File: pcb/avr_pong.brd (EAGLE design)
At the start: 61.3 x 58.4 mm, 20 parts, among them IC1 7805TV, J1 DCJ0202, U1 ATMEGA328P_PDIP, Y1 16 MHz

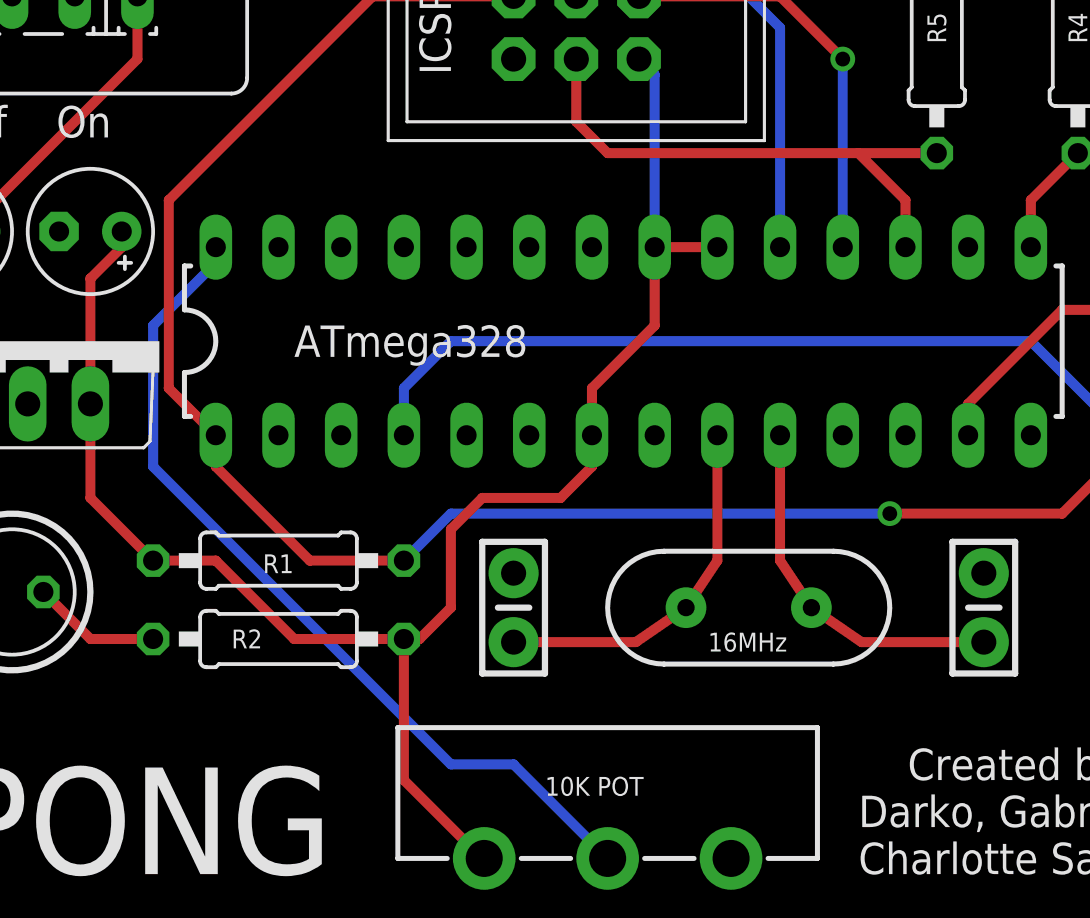
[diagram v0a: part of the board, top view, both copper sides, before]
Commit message: Updated board layout.
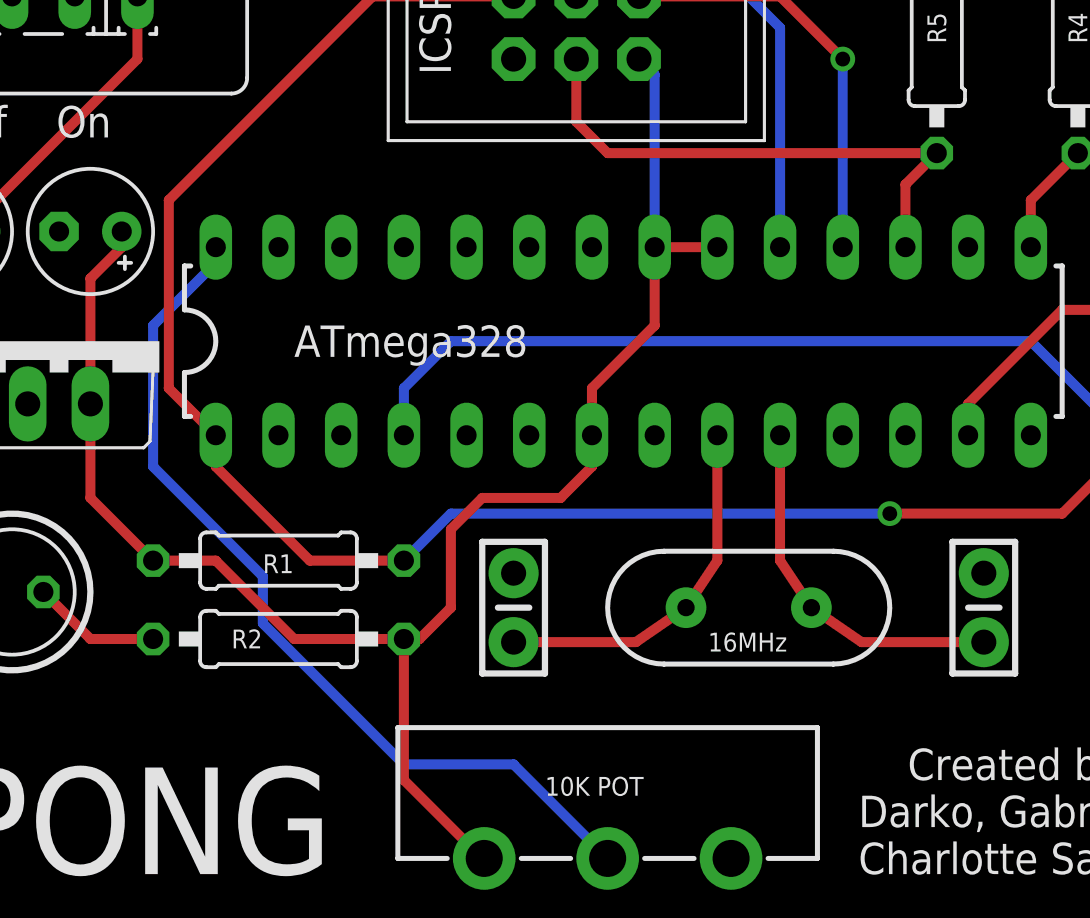
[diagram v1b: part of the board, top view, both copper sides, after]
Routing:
- net N$7: track 34.9 -> 36.0 mm
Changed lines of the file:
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@@
 <contactref element="U1" pad="17"/>
 <contactref element="R5" pad="1"/>
-<wire x1="43.815" y1="31.115" x2="40.64" y2="31.115" width="0.4064" layer="1"/>
-<wire x1="40.64" y1="31.115" x2="30.48" y2="31.115" width="0.4064" layer="1"/>
+<wire x1="43.815" y1="31.115" x2="30.48" y2="31.115" width="0.4064" layer="1"/>
 <wire x1="30.48" y1="31.115" x2="29.21" y2="32.385" width="0.4064" layer="1"/>
 <wire x1="29.21" y1="32.385" x2="29.21" y2="34.925" width="0.4064" layer="1"/>
-<wire x1="42.545" y1="27.305" x2="42.545" y2="29.21" width="0.4064" layer="1"/>
-<wire x1="42.545" y1="29.21" x2="40.64" y2="31.115" width="0.4064" layer="1"/>
+<wire x1="42.545" y1="27.305" x2="42.545" y2="29.845" width="0.4064" layer="1"/>
+<wire x1="42.545" y1="29.845" x2="43.815" y2="31.115" width="0.4064" layer="1"/>
 </signal>
 <signal name="MISO">
@@
 <wire x1="12.065" y1="24.13" x2="14.605" y2="26.67" width="0.4064" layer="16"/>
 <wire x1="14.605" y1="26.67" x2="14.605" y2="27.305" width="0.4064" layer="16"/>
-<wire x1="26.67" y1="6.35" x2="24.13" y2="6.35" width="0.4064" layer="16"/>
-<wire x1="24.13" y1="6.35" x2="12.065" y2="18.415" width="0.4064" layer="16"/>
+<wire x1="26.67" y1="6.35" x2="22.225" y2="6.35" width="0.4064" layer="16"/>
+<wire x1="22.225" y1="6.35" x2="16.51" y2="12.065" width="0.4064" layer="16"/>
+<wire x1="16.51" y1="12.065" x2="16.51" y2="13.97" width="0.4064" layer="16"/>
+<wire x1="16.51" y1="13.97" x2="12.065" y2="18.415" width="0.4064" layer="16"/>
 </signal>
 </signals>

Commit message: Added PCB layout.
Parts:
- removed J1: DCJ0202, con-jack:DCJ0202
- added JP1: POWER_JACKPTH, SparkFun-Connectors:POWER_JACK_PTH
- S1: value (none) -> Black
- moved C3 1.27 mm to (3.81, 29.2)
- moved C4 1.27 mm to (9.53, 29.2)
- moved S1 1.27 mm to (8.89, 38.7)
- moved IC1 0.90 mm to (6.35, 24.1)
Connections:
- net GND: now also JP1.GND, JP1.GNDBREAK; no longer J1.2, J1.3
- net N$6: now also JP1.PWR; no longer J1.1
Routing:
- net +5V: track 69.4 -> 71.2 mm
- net N$6: track 7.97 -> 9.24 mm
- net N$5: track 19.4 -> 20.3 mm
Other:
- board text added: "RCA Jack"
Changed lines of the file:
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@@
 <text x="59.69" y="45.085" size="1.27" layer="21" font="vector" rot="R90">April 2015</text>
 <text x="2.54" y="10.795" size="1.27" layer="21" font="vector" rot="R90">Power</text>
-<text x="3.81" y="31.75" size="1.27" layer="21" font="vector">Off    On</text>
+<text x="4.445" y="33.02" size="1.27" layer="21" font="vector">Off    On</text>
 <text x="24.13" y="34.29" size="1.27" layer="21" font="vector" rot="R90">ICSP</text>
 <text x="17.78" y="22.86" size="1.27" layer="21" font="vector">ATmega328</text>
@@
 Charlotte Sancanin</text>
 <text x="45.085" y="55.245" size="1.27" layer="22" font="vector" rot="MR0">Revision 1.0   April 2015</text>
-<text x="13.97" y="46.355" size="1.27" layer="21" font="vector" rot="R90">7-12 VDC</text>
+<text x="14.986" y="48.26" size="1.27" layer="21" font="vector" rot="R90">7-12 VDC</text>
+<text x="38.1" y="47.625" size="0.762" layer="21" font="vector">RCA Jack</text>
 </plain>
 <attributes>
@@
 <element name="C1" library="SparkFun-Capacitors" package="CAP-PTH-SMALL-KIT" value="22pf" x="26.67" y="12.7" rot="R90"/>
 <element name="C2" library="SparkFun-Capacitors" package="CAP-PTH-SMALL-KIT" value="22pf" x="45.72" y="12.7" rot="R90"/>
-<element name="C3" library="rcl" package="E2,5-5" value="10uF" x="3.81" y="27.94" smashed="yes" rot="R180"/>
-<element name="C4" library="rcl" package="E2,5-5" value="10uF" x="9.525" y="27.94" smashed="yes" rot="R180"/>
-<element name="IC1" library="linear" package="TO220V" value="7805TV" x="6.985" y="23.495" smashed="yes"/>
+<element name="C3" library="rcl" package="E2,5-5" value="10uF" x="3.81" y="29.21" smashed="yes" rot="R180"/>
+<element name="C4" library="rcl" package="E2,5-5" value="10uF" x="9.525" y="29.21" smashed="yes" rot="R180"/>
+<element name="IC1" library="linear" package="TO220V" value="7805TV" x="6.35" y="24.13" smashed="yes"/>
 <element name="ICSP" library="adaprog" package="ISP6" value="PINHD-2X3THM" x="29.21" y="36.195" smashed="yes" rot="R180"/>
-<element name="J1" library="con-jack" package="DCJ0202" value="DCJ0202" x="7.62" y="48.006" smashed="yes" rot="R180">
-<attribute name="OC_NEWARK" value="unknown" x="7.62" y="48.006" size="1.778" layer="27" rot="R180" display="off"/>
-<attribute name="MPN" value="" x="7.62" y="48.006" size="1.778" layer="27" rot="R180" display="off"/>
-<attribute name="MF" value="" x="7.62" y="48.006" size="1.778" layer="27" rot="R180" display="off"/>
-<attribute name="OC_FARNELL" value="unknown" x="7.62" y="48.006" size="1.778" layer="27" rot="R180" display="off"/>
-</element>
 <element name="LED1" library="led" package="LED5MM" value="GREEN" x="6.35" y="13.335" smashed="yes" rot="R180"/>
 <element name="R1" library="rcl" package="0207/10" value="10k" x="17.145" y="14.605" smashed="yes"/>
@@
 </element>
 <element name="RV1" library="SparkFun-Electromechanical" package="POT_ALPHA_RV16AF-20" value="10K" x="30.48" y="2.54" smashed="yes"/>
-<element name="S1" library="switch" package="M251" value="" x="8.89" y="37.465" smashed="yes" rot="R180">
-<attribute name="VALUE" x="14.605" y="40.767" size="1.27" layer="27" ratio="10" rot="R180"/>
-</element>
+<element name="S1" library="switch" package="M251" value="Black" x="8.89" y="38.735" smashed="yes" rot="R180"/>
 <element name="U1" library="SparkFun-DigitalIC" package="DIL28-3" value="ATMEGA328P_PDIP" x="31.115" y="23.495" smashed="yes"/>
 <element name="Y1" library="SparkFun-FreqCtrl" package="HC49US" value="16 MHz" x="36.195" y="12.7" smashed="yes" rot="R180"/>
 <element name="U$1" library="3-rca-jack" package="3-RCA-JACK" value="3-RCA-JACK" x="26.67" y="44.45" smashed="yes"/>
+<element name="JP1" library="SparkFun-Connectors" package="POWER_JACK_PTH" value="POWER_JACKPTH" x="8.382" y="61.468" smashed="yes" rot="R180">
+<attribute name="PROD_ID" value="CONN-08197" x="8.382" y="61.468" size="1.778" layer="27" rot="R180" display="off"/>
+</element>
 </elements>
 <signals>
@@
 <contactref element="C4" pad="-"/>
 <contactref element="LED1" pad="K"/>
-<contactref element="J1" pad="3"/>
-<contactref element="J1" pad="2"/>
 <contactref element="RESET" pad="2"/>
 <contactref element="SELECT" pad="4"/>
@@
 <vertex x="61.595" y="58.42"/>
 </polygon>
+<contactref element="JP1" pad="GND"/>
+<contactref element="JP1" pad="GNDBREAK"/>
 </signal>
 <signal name="+5V">
@@
 <wire x1="22.225" y1="5.715" x2="22.225" y2="11.43" width="0.4064" layer="1"/>
 <wire x1="34.925" y1="27.305" x2="32.385" y2="27.305" width="0.4064" layer="1"/>
-<wire x1="12.065" y1="14.605" x2="9.525" y2="17.145" width="0.4064" layer="1"/>
-<wire x1="9.525" y1="17.145" x2="9.525" y2="20.955" width="0.4064" layer="1"/>
 <wire x1="22.225" y1="11.43" x2="17.78" y2="11.43" width="0.4064" layer="1"/>
 <wire x1="17.78" y1="11.43" x2="14.605" y2="14.605" width="0.4064" layer="1"/>
@@
 <wire x1="24.13" y1="12.7" x2="22.86" y2="11.43" width="0.4064" layer="1"/>
 <wire x1="22.86" y1="11.43" x2="22.225" y2="11.43" width="0.4064" layer="1"/>
-<wire x1="9.525" y1="20.955" x2="9.525" y2="26.035" width="0.4064" layer="1"/>
 <wire x1="32.385" y1="27.305" x2="32.385" y2="34.29" width="0.4064" layer="16"/>
 <wire x1="32.385" y1="34.29" x2="31.75" y2="34.925" width="0.4064" layer="16"/>
-<wire x1="9.525" y1="26.035" x2="10.795" y2="27.305" width="0.4064" layer="1"/>
-<wire x1="10.795" y1="27.305" x2="10.795" y2="27.94" width="0.4064" layer="1"/>
 <wire x1="25.4" y1="2.54" x2="22.225" y2="5.715" width="0.4064" layer="1"/>
+<wire x1="8.89" y1="21.59" x2="8.89" y2="26.035" width="0.4064" layer="1"/>
+<wire x1="8.89" y1="26.035" x2="10.795" y2="27.94" width="0.4064" layer="1"/>
+<wire x1="10.795" y1="27.94" x2="10.795" y2="29.21" width="0.4064" layer="1"/>
+<wire x1="8.89" y1="21.59" x2="8.89" y2="17.78" width="0.4064" layer="1"/>
+<wire x1="8.89" y1="17.78" x2="12.065" y2="14.605" width="0.4064" layer="1"/>
 </signal>
 <signal name="MOSI">
@@
 <wire x1="58.4962" y1="22.5044" x2="51.9938" y2="22.5044" width="0.4064" layer="1"/>
 <wire x1="26.67" y1="37.465" x2="20.955" y2="37.465" width="0.4064" layer="1"/>
-<wire x1="20.955" y1="37.465" x2="12.7" y2="29.21" width="0.4064" layer="1"/>
-<wire x1="12.7" y1="29.21" x2="12.7" y2="21.59" width="0.4064" layer="1"/>
 <wire x1="12.7" y1="21.59" x2="14.605" y2="19.685" width="0.4064" layer="1"/>
+<wire x1="12.7" y1="21.59" x2="12.7" y2="29.21" width="0.4064" layer="1"/>
+<wire x1="12.7" y1="29.21" x2="20.955" y2="37.465" width="0.4064" layer="1"/>
 </signal>
 <signal name="N$5">
@@
 <contactref element="C3" pad="+"/>
 <contactref element="S1" pad="1"/>
-<wire x1="11.43" y1="37.465" x2="11.43" y2="34.925" width="0.4064" layer="1"/>
-<wire x1="11.43" y1="34.925" x2="5.08" y2="28.575" width="0.4064" layer="1"/>
-<wire x1="5.08" y1="28.575" x2="5.08" y2="27.94" width="0.4064" layer="1"/>
-<wire x1="4.445" y1="20.955" x2="4.445" y2="26.67" width="0.4064" layer="1"/>
-<wire x1="4.445" y1="26.67" x2="5.08" y2="27.305" width="0.4064" layer="1"/>
-<wire x1="5.08" y1="27.305" x2="5.08" y2="27.94" width="0.4064" layer="1"/>
+<wire x1="5.08" y1="29.21" x2="5.08" y2="27.94" width="0.4064" layer="1"/>
+<wire x1="5.08" y1="27.94" x2="3.81" y2="26.67" width="0.4064" layer="1"/>
+<wire x1="3.81" y1="26.67" x2="3.81" y2="21.59" width="0.4064" layer="1"/>
+<wire x1="11.43" y1="38.735" x2="11.43" y2="36.83" width="0.4064" layer="1"/>
+<wire x1="11.43" y1="36.83" x2="5.08" y2="30.48" width="0.4064" layer="1"/>
+<wire x1="5.08" y1="30.48" x2="5.08" y2="29.21" width="0.4064" layer="1"/>
 </signal>
 <signal name="N$8">
@@
 <wire x1="12.065" y1="11.43" x2="9.525" y2="11.43" width="0.4064" layer="1"/>
 <wire x1="9.525" y1="11.43" x2="7.62" y2="13.335" width="0.4064" layer="1"/>
-</signal>
-<signal name="N$6">
-<contactref element="J1" pad="1"/>
-<contactref element="S1" pad="2"/>
-<wire x1="7.62" y1="44.906" x2="7.62" y2="41.275" width="0.4064" layer="1"/>
-<wire x1="7.62" y1="41.275" x2="8.89" y2="40.005" width="0.4064" layer="1"/>
-<wire x1="8.89" y1="40.005" x2="8.89" y2="37.465" width="0.4064" layer="1"/>
 </signal>
 <signal name="N$1">
@@
 <wire x1="16.51" y1="13.97" x2="12.065" y2="18.415" width="0.4064" layer="16"/>
 </signal>
+<signal name="N$6">
+<contactref element="S1" pad="2"/>
+<contactref element="JP1" pad="PWR"/>
+<wire x1="8.89" y1="38.735" x2="8.89" y2="47.26" width="0.4064" layer="1"/>
+<wire x1="8.89" y1="47.26" x2="8.382" y2="47.768" width="0.4064" layer="1"/>
+</signal>
 </signals>
